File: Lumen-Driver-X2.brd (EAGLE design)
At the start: 60 x 55 mm, 30 parts, among them J1 AVR_SPI_PRG_6PTH, U1 Tiny45-20-SMT, Y1 8Mhz

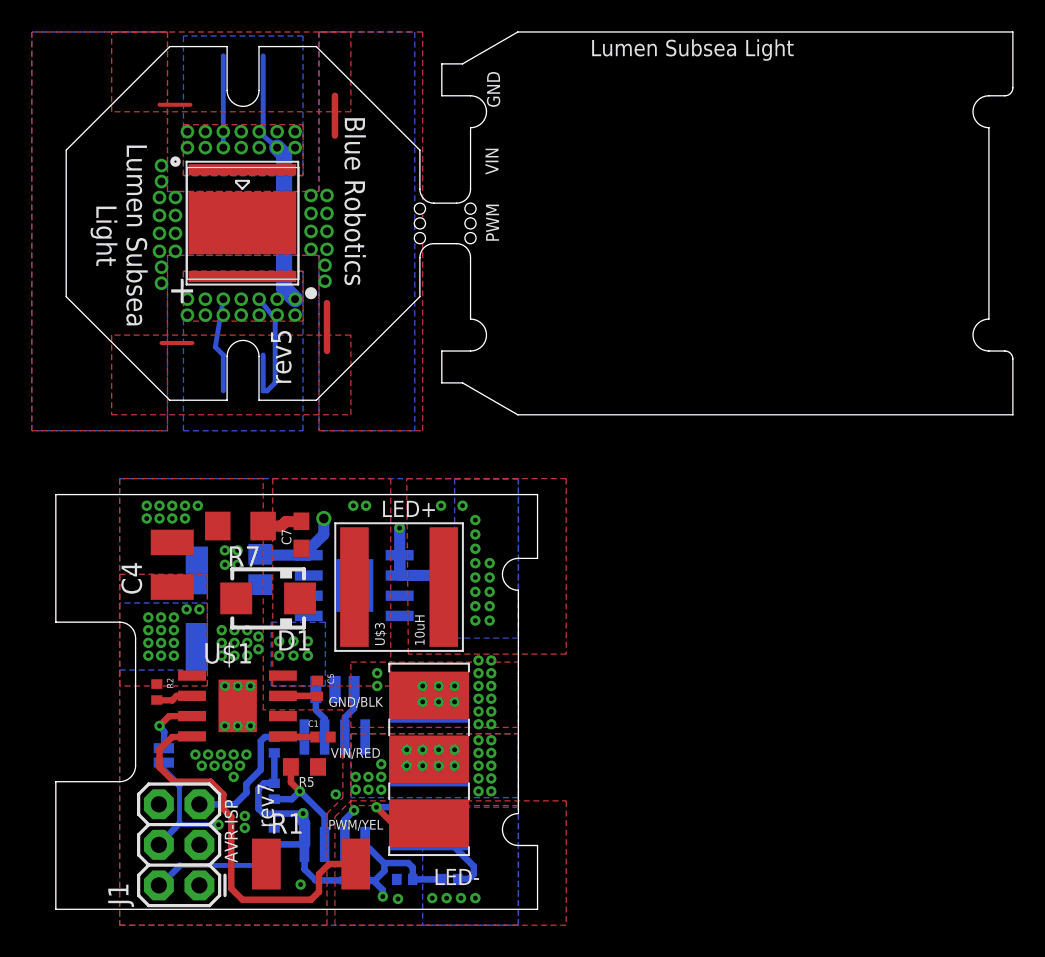
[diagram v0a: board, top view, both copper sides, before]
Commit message: Updated R2 design. Ordered and tested.
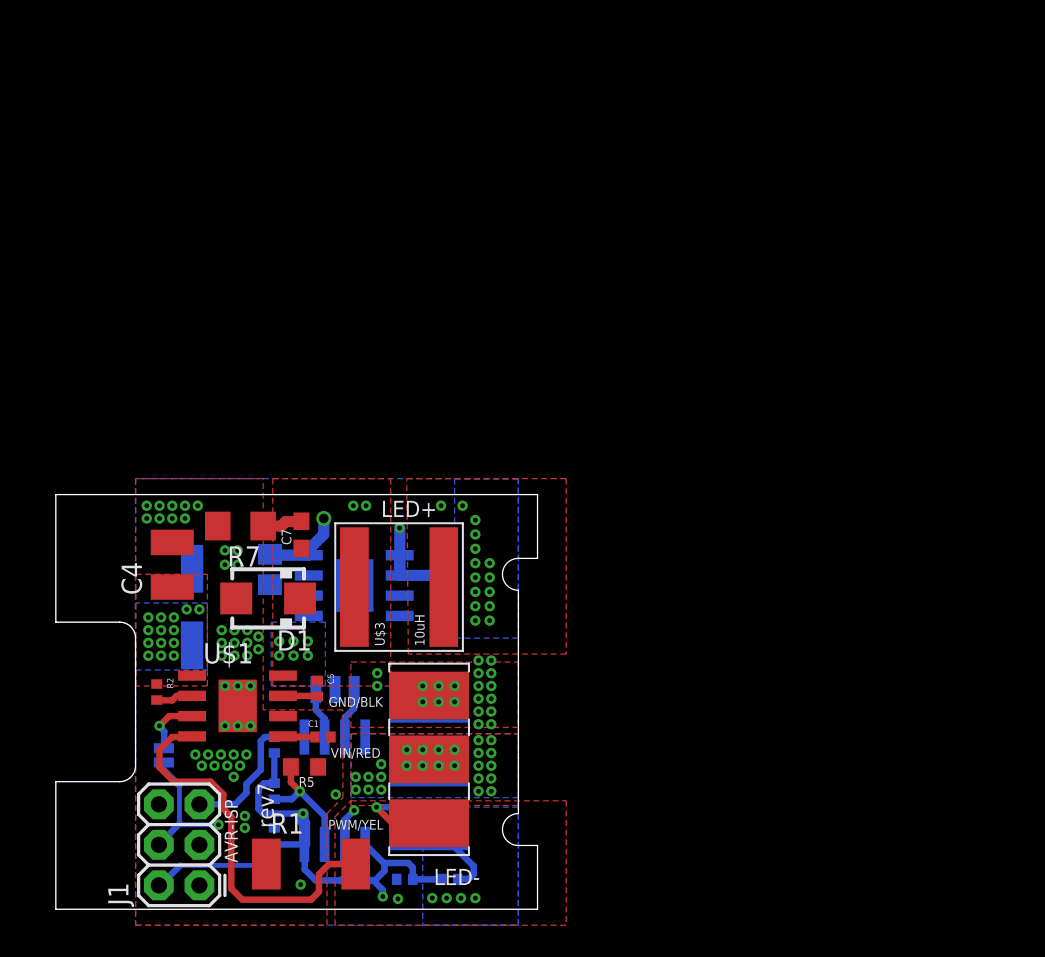
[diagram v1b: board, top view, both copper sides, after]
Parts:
- removed C2: 0.68uF 100V, resistor:C0805
- removed U$10: LOGOBR-LOGO-MS-COPPER, BlueRobotics-Main:BR-LOGO-MEDIUM-SMALL-COPPER
- removed U$2: LED-MK-R, BlueRobotics-Main:MK-R
- moved C9 0.60 mm to (13.4, 21.3)
- moved C3 0.32 mm to (8.54, 18.9)
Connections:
- removed net EXT: U$2.EXP
- removed net LED+ISO: C2.2, U$2.A
- removed net LED-ISO: C2.1, U$2.C
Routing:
- net LED-ISO: track 18.9 -> 0.00 mm, vias 14 -> 0
- net LED+ISO: track 15.8 -> 0.00 mm, vias 14 -> 0
- net EXT: track 9.38 -> 0.00 mm, vias 22 -> 0
- net VIN: track 7.15 -> 6.53 mm
- removed copper zone on layer 1, net EXT
- removed copper zone on layer 15, net EXT
- removed copper zone on layer 16, net EXT
- removed copper zone on layer 2, net EXT
- removed copper zone on layer 1, net LED+ISO
- removed copper zone on layer 16, net LED+ISO
- removed copper zone on layer 1, net LED-ISO
- removed copper zone on layer 16, net LED-ISO
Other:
- board size 60 x 55 mm -> 30.2 x 26 mm
- board text removed: "+"
- board text removed: "Blue Robotics"
- board text removed: "BlueRobotics"
- board text removed: "Daisy chain pads"
- board text removed: "GND"
- board text removed: "Lumen Subsea Light"
- board text removed: "PWM"
- board text removed: "VIN"
- board text removed: "rev5"

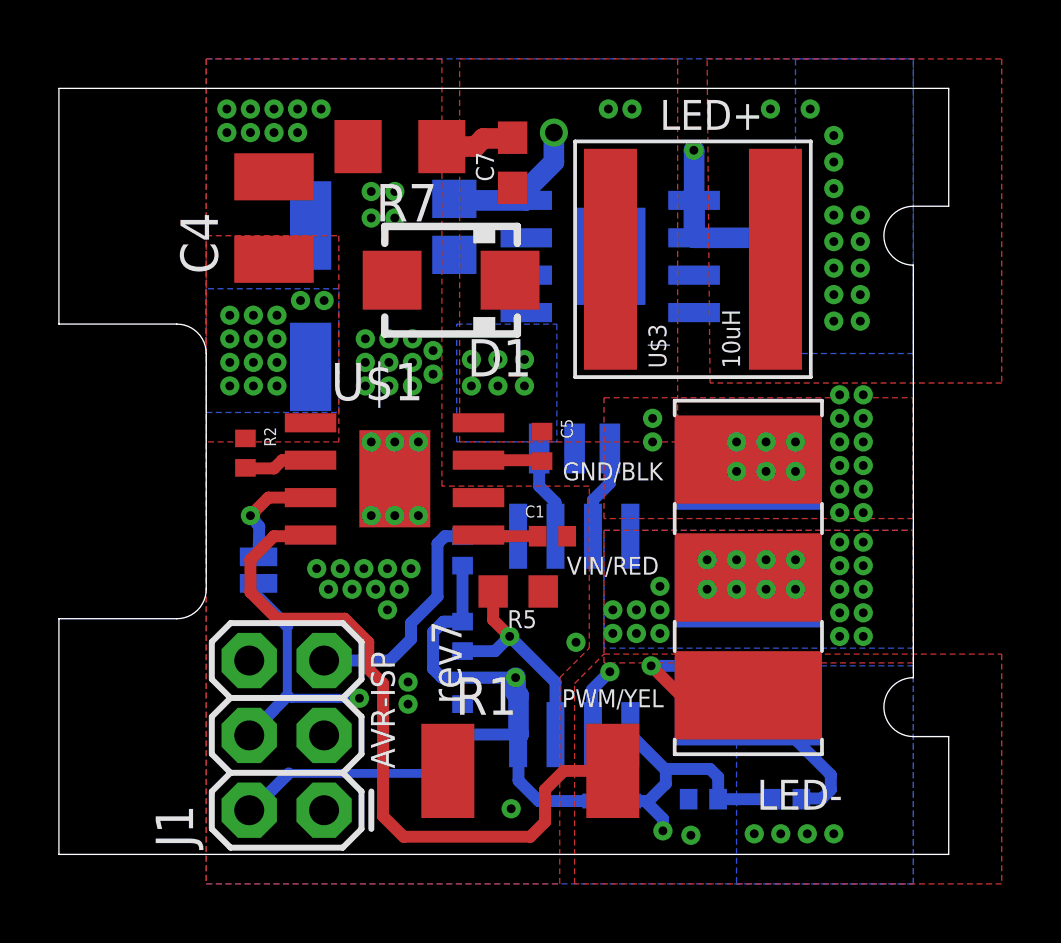
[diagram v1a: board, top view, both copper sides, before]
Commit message: updated driver.
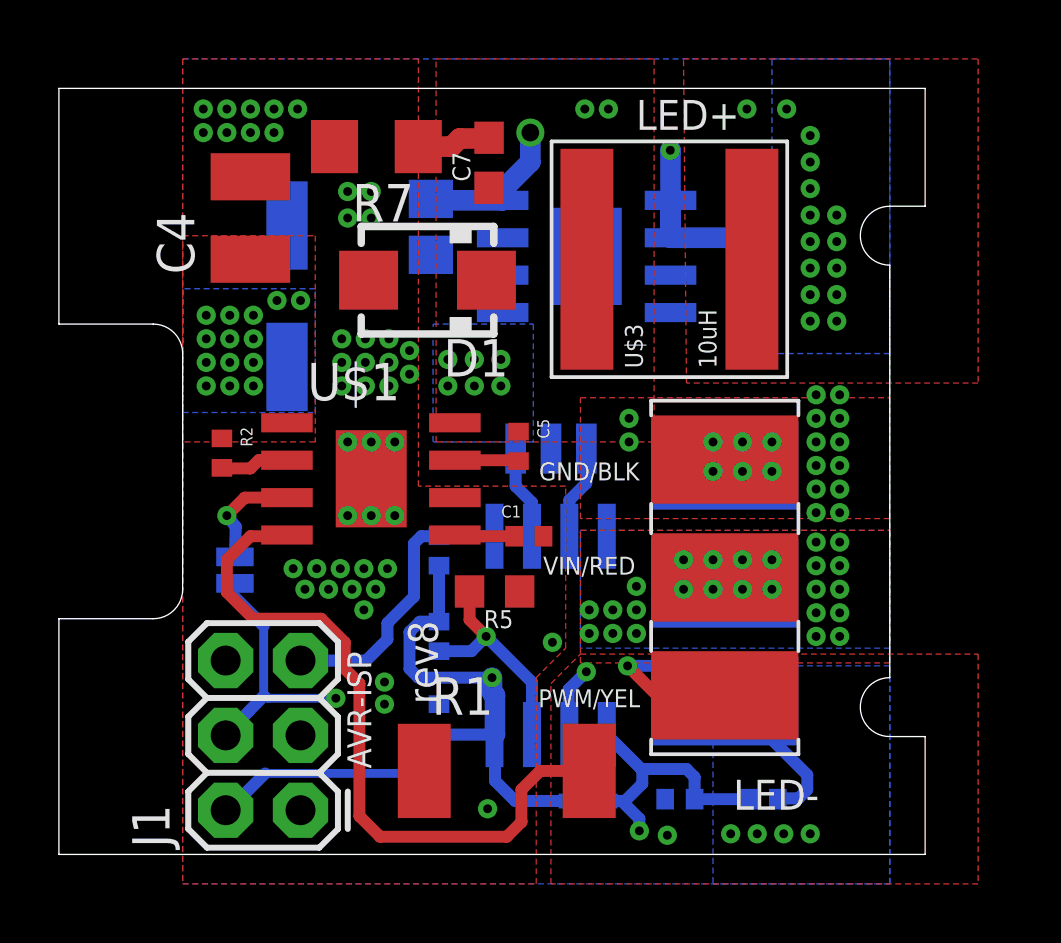
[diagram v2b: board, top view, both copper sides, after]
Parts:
- moved C1 0.80 mm to (15.9, 10.8)
- moved C3 0.80 mm to (7.74, 18.9)
- moved C7 0.80 mm to (14.6, 23.5)
- moved C9 0.80 mm to (12.6, 21.3)
- moved D1 0.80 mm to (12.5, 19.5)
- moved J1 0.80 mm to (8.20, 1.50)
- moved R1 0.80 mm to (15.2, 2.83)
- moved R5 0.80 mm to (14.8, 8.93)
- moved R6 0.80 mm to (23.9, 1.88)
- moved R8 0.80 mm to (21.1, 1.88)
- moved SJ1 0.80 mm to (5.97, 9.65)
- moved U$1 0.80 mm to (10.6, 12.8)
- moved U$13 0.80 mm to (17.9, 20.3)
- moved U$3 0.80 mm to (20.7, 20.2)
- moved C4 0.80 mm to (6.50, 21.6)
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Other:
- board size 30.2 x 26 mm -> 29.4 x 26 mm
- board text added: "rev8"
- board text removed: "rev7"
